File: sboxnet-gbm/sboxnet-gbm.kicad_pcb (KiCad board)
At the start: 2 copper layers, 102.4 x 85.1 mm, 47 parts, among them J1 Screw_Terminal_01x04, J2 Screw_Terminal_01x04, J3 Screw_Terminal_01x04, J4 sboxnet-stecker_02x17, J5 Screw_Terminal_01x04, U1 LTV-844, U2 LTV-844, U3 LTV-844, U4 SN65HVD230

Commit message: gbm
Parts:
- removed REF** (x4): MountingHole_2.2mm_M2, sboxnet:MountingHole_2.2mm_M2
- removed RN2: R_Network05, Resistor_THT:R_Array_SIP6
- removed TH0: Thermistor_PTC, Resistor_SMD:R_1206_3216Metric
- added J6: Conn_02x08_Top_Bottom, Connector_PinSocket_2.54mm:PinSocket_2x08_P2.54mm_Vertical, F.Cu at (136.9, 124.8)
- added JP1: SolderJumper_3_Open, Jumper:SolderJumper-3_P1.3mm_Open_RoundedPad1.0x1.5mm, F.Cu at (232.8, 67.2)
- added JP2: SolderJumper_3_Open, Jumper:SolderJumper-3_P1.3mm_Open_RoundedPad1.0x1.5mm, F.Cu at (183.1, 62.5)
- added JP3: SolderJumper_3_Open, Jumper:SolderJumper-3_P1.3mm_Open_RoundedPad1.0x1.5mm, F.Cu at (183.1, 66.3)
- added TH10: Thermistor_PTC, Resistor_SMD:R_1206_3216Metric, F.Cu at (263.6, 41.8)
- added TP10: TestPoint, Connector_PinHeader_2.54mm:PinHeader_1x01_P2.54mm_Vertical, F.Cu at (250.2, 59.1)
- added TP2: TestPoint, Connector_PinHeader_2.54mm:PinHeader_1x01_P2.54mm_Vertical, F.Cu at (263.1, 49.1)
- added TP3: TestPoint, Connector_PinHeader_2.54mm:PinHeader_1x01_P2.54mm_Vertical, F.Cu at (256.5, 55.8)
- added TP4: TestPoint, Connector_PinHeader_2.54mm:PinHeader_1x01_P2.54mm_Vertical, F.Cu at (250.2, 63.7)
- added TP5: TestPoint, Connector_PinHeader_2.54mm:PinHeader_1x01_P2.54mm_Vertical, F.Cu at (274.7, 35.9)
- added TP6: TestPoint, Connector_PinHeader_2.54mm:PinHeader_1x01_P2.54mm_Vertical, F.Cu at (268.8, 42.5)
- added TP7: TestPoint, Connector_PinHeader_2.54mm:PinHeader_1x01_P2.54mm_Vertical, F.Cu at (238.1, 71.0)
- added TP8: TestPoint, Connector_PinHeader_2.54mm:PinHeader_1x01_P2.54mm_Vertical, F.Cu at (226.7, 81.7)
- added TP9: TestPoint, Connector_PinHeader_2.54mm:PinHeader_1x01_P2.54mm_Vertical, F.Cu at (215.4, 93.7)
- BAR1: footprint Display:HDSP-4830 -> Package_DIP:DIP-20_W7.62mm_Socket
- D1, D10, D2, D3, D4, D5, D6, D7, D8, D9, TH1, TH2, TH3, TH4, TH5, TH6, TH7, TH8, TH9, U4: moved to F.Cu
- R1, R10, R2, R3, R4, R5, R6, R7, R8, R9: footprint Resistor_SMD:R_1206_3216Metric_Pad1.42x1.75mm_HandSolder -> Resistor_SMD:R_1206_3216Metric_Pad1.30x1.75mm_HandSolder; moved to F.Cu
- RN1: value R_Network05 -> R_Network15; footprint Resistor_THT:R_Array_SIP6 -> Package_SO:SOIC-16W_5.3x10.2mm_P1.27mm; moved to B.Cu
- moved TH7 217.8 mm to (269.6, 35.2), turned to 0 degrees
- moved D6 199.1 mm to (254.7, 48.5)
- moved TH6 199.0 mm to (263.6, 38.5), turned to 0 degrees
- moved TP1 182.9 mm to (244.6, 64.4)
- moved R6 175.8 mm to (233.0, 49.2), turned to 0 degrees
- moved TH3 160.8 mm to (263.6, 45.1), turned to 0 degrees
- moved U1 159.6 mm to (220.8, 49.6), turned to 0 degrees
- moved D3 153.4 mm to (236.2, 60.5)
- moved TH1 152.6 mm to (269.2, 38.5), turned to 0 degrees
- moved TH4 143.3 mm to (238.5, 67.1), turned to 0 degrees
- moved D5 134.1 mm to (205.1, 74.9)
- moved R7 130.4 mm to (263.8, 35.2)
- moved J3 128.3 mm to (218.8, 40.6)
- moved TH2 127.4 mm to (245.1, 60.4), turned to 0 degrees
- moved TH5 126.4 mm to (210.2, 91.5), turned to 0 degrees
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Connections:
- BAR1 pad 1: PD0 -> PC7
- BAR1 pad 10: PC7 -> PD0
- BAR1 pad 11: Net-(BAR1-Pad11) -> /L10
- BAR1 pad 12: Net-(BAR1-Pad12) -> /L9
- BAR1 pad 13: Net-(BAR1-Pad13) -> /L8
- BAR1 pad 14: Net-(BAR1-Pad14) -> /L7
- BAR1 pad 15: Net-(BAR1-Pad15) -> /L6
- BAR1 pad 16: Net-(BAR1-Pad16) -> /L5
- BAR1 pad 17: Net-(BAR1-Pad17) -> /L4
- BAR1 pad 18: Net-(BAR1-Pad18) -> /L3
- BAR1 pad 19: Net-(BAR1-Pad19) -> /L2
- BAR1 pad 2: PD1 -> PC6
- BAR1 pad 20: Net-(BAR1-Pad20) -> /L1
- BAR1 pad 3: PD2 -> PD7
- BAR1 pad 4: PD3 -> PD6
- BAR1 pad 5: PD4 -> PD5
- BAR1 pad 6: PD5 -> PD4
- BAR1 pad 7: PD6 -> PD3
- BAR1 pad 8: PD7 -> PD2
- BAR1 pad 9: PC6 -> PD1
- J4 pad 1: Net-(J4-Pad1) -> unconnected-(J4-Pad1)
- J4 pad 13: DCC_SENS -> PB0
- J4 pad 14: +3V3 -> PB1
- J4 pad 15: GNDPWR -> PB2
- J4 pad 16: +3V3 -> unconnected-(J4-Pad16)
- J4 pad 19: Net-(J4-Pad19) -> unconnected-(J4-Pad19)
- J4 pad 20: Net-(J4-Pad20) -> unconnected-(J4-Pad20)
- J4 pad 21: Net-(J4-Pad21) -> DCC_SENS
- J4 pad 22: Net-(J4-Pad22) -> unconnected-(J4-Pad22)
- J4 pad 4: Net-(J4-Pad4) -> unconnected-(J4-Pad4)
- J5 pad 3: Net-(J5-Pad3) -> unconnected-(J5-Pad3)
- J5 pad 4: Net-(J5-Pad4) -> unconnected-(J5-Pad4)
- R3 pad 2: Net-(D4-Pad3) -> Net-(D3-Pad3)
- R4 pad 2: Net-(D5-Pad3) -> Net-(D4-Pad3)
- R5 pad 2: Net-(D3-Pad3) -> Net-(D5-Pad3)
- RN1 pad 1: GNDPWR -> /L1
- RN1 pad 2: Net-(BAR1-Pad20) -> /L2
- RN1 pad 3: Net-(BAR1-Pad19) -> /L3
- RN1 pad 4: Net-(BAR1-Pad18) -> /L4
- RN1 pad 5: Net-(BAR1-Pad17) -> /L5
- RN1 pad 6: Net-(BAR1-Pad16) -> /L6
- TH1 pad 1: Net-(D8-Pad3) -> Net-(D1-Pad3)
- TH1 pad 2: S6 -> S0
- TH2 pad 2: S5 -> S1
- TH3 pad 1: Net-(D1-Pad3) -> Net-(D3-Pad3)
- TH3 pad 2: S4 -> S2
- TH5 pad 1: Net-(D3-Pad3) -> Net-(D5-Pad3)
- TH5 pad 2: S2 -> S4
- TH6 pad 1: Net-(D5-Pad3) -> Net-(D6-Pad3)
- TH6 pad 2: S1 -> S5
- TH7 pad 1: Net-(D6-Pad3) -> Net-(D7-Pad3)
- TH7 pad 2: S0 -> S6
- TH8 pad 1: Net-(D9-Pad3) -> Net-(D8-Pad3)
- TH8 pad 2: S9 -> S7
- TH9 pad 1: Net-(D10-Pad3) -> Net-(D9-Pad3)
- U1 pad 1: Net-(R6-Pad1) -> Net-(R1-Pad1)
- U1 pad 3: Net-(R4-Pad1) -> Net-(R2-Pad1)
- U1 pad 5: Net-(R5-Pad1) -> Net-(R3-Pad1)
- U1 pad 7: Net-(R3-Pad1) -> Net-(R4-Pad1)
- U2 pad 1: Net-(R1-Pad1) -> Net-(R5-Pad1)
- U2 pad 3: Net-(R2-Pad1) -> Net-(R6-Pad1)
- U2 pad 5: Net-(R8-Pad1) -> Net-(R7-Pad1)
- U2 pad 7: Net-(R7-Pad1) -> Net-(R8-Pad1)
- U3 pad 1: Net-(R10-Pad1) -> Net-(R9-Pad1)
- U3 pad 10: (no net) -> unconnected-(U3-Pad10)
- U3 pad 11: (no net) -> unconnected-(U3-Pad11)
- U3 pad 12: (no net) -> unconnected-(U3-Pad12)
- U3 pad 3: Net-(R9-Pad1) -> Net-(R10-Pad1)
- U3 pad 5: (no net) -> unconnected-(U3-Pad5)
- U3 pad 6: (no net) -> unconnected-(U3-Pad6)
- U3 pad 7: (no net) -> unconnected-(U3-Pad7)
- U3 pad 8: (no net) -> unconnected-(U3-Pad8)
- U3 pad 9: (no net) -> unconnected-(U3-Pad9)
- U4 pad 1: Net-(U4-Pad1) -> unconnected-(U4-Pad1)
- U4 pad 5: Net-(U4-Pad5) -> unconnected-(U4-Pad5)
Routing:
- net SGND1: track 430.8 -> 0.00 mm
- net GNDPWR: track 275.2 -> 78.1 mm
- net PD5: track 45.6 -> 121.3 mm
- net PD4: track 41.7 -> 114.8 mm
- net PD3: track 43.4 -> 110.0 mm, vias 0 -> 1
- net PD2: track 39.3 -> 105.3 mm
- net +3V3: track 56.7 -> 0.00 mm
- net PC1: track 55.0 -> 0.00 mm
- net PC0: track 48.1 -> 0.00 mm
- net DCC_SENS: track 42.5 -> 0.00 mm
- net Net-(R10-Pad1): track 40.2 -> 0.00 mm
- net S0: track 38.3 -> 0.00 mm
- net Net-(D8-Pad3): track 37.9 -> 0.00 mm
- net PA7: track 37.5 -> 0.00 mm
- net Net-(D7-Pad3): track 34.5 -> 0.00 mm
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- removed copper zone on B.Cu, net GNDPWR
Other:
- board outline removed
- net class Default removed
- rule pad_to_mask_clearance: 0.051 -> 0
- board text removed: "(c) 09.07.2020 Thomas Maier"
- board text removed: "0"
- board text removed: "1"
- board text removed: "2"
- board text removed: "3"
- board text removed: "4"
- board text removed: "5"
- board text removed: "6"
- board text removed: "7"
- board text removed: "8"
- board text removed: "9"
- board text removed: "SGND"
- board text removed: "Sboxnet GBM 2"
- board text removed: "tom@tom.ist-im-web.de"

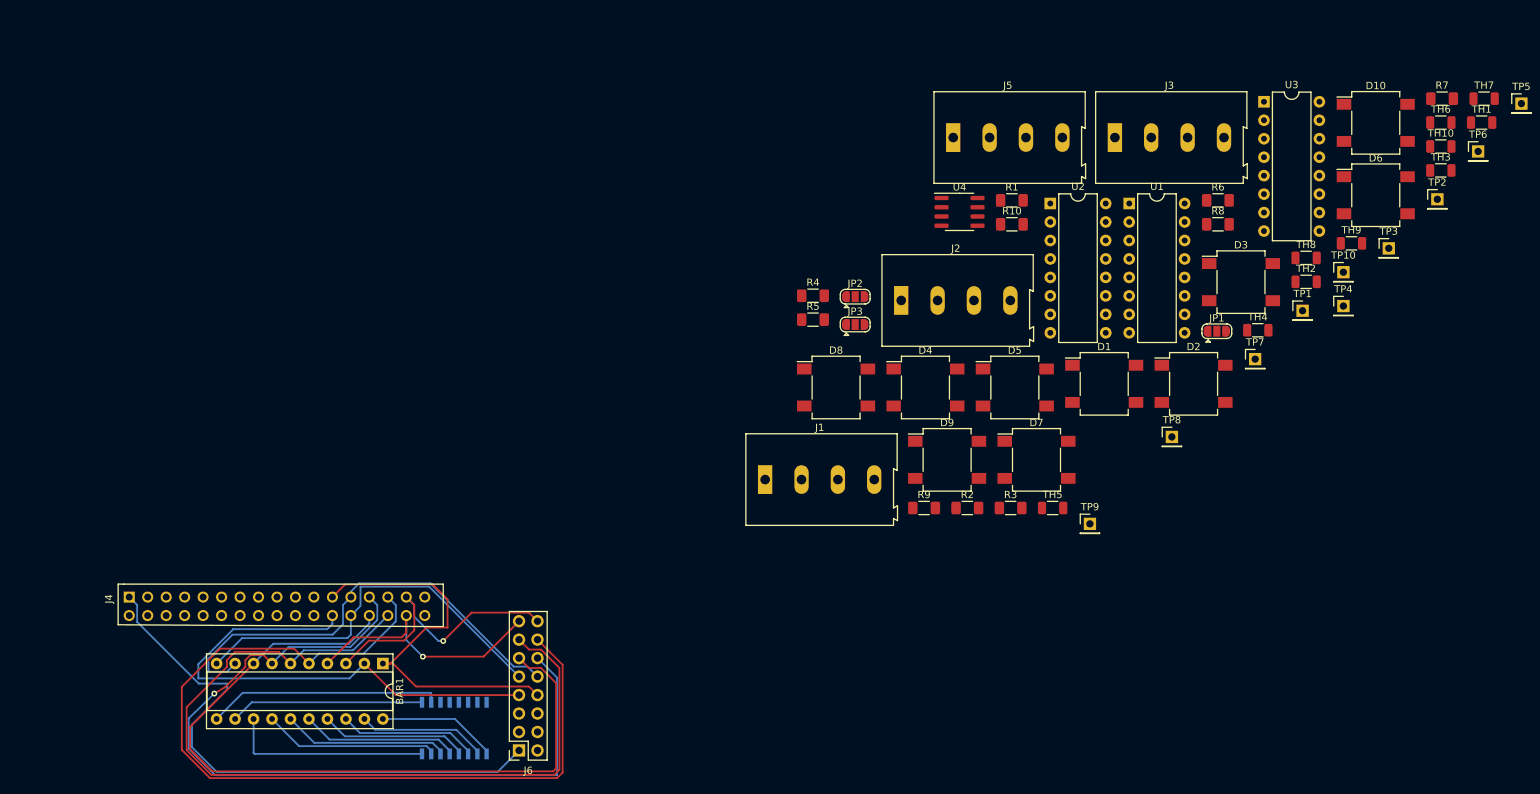
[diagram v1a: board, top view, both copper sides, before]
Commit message: kicad 5 -> 6
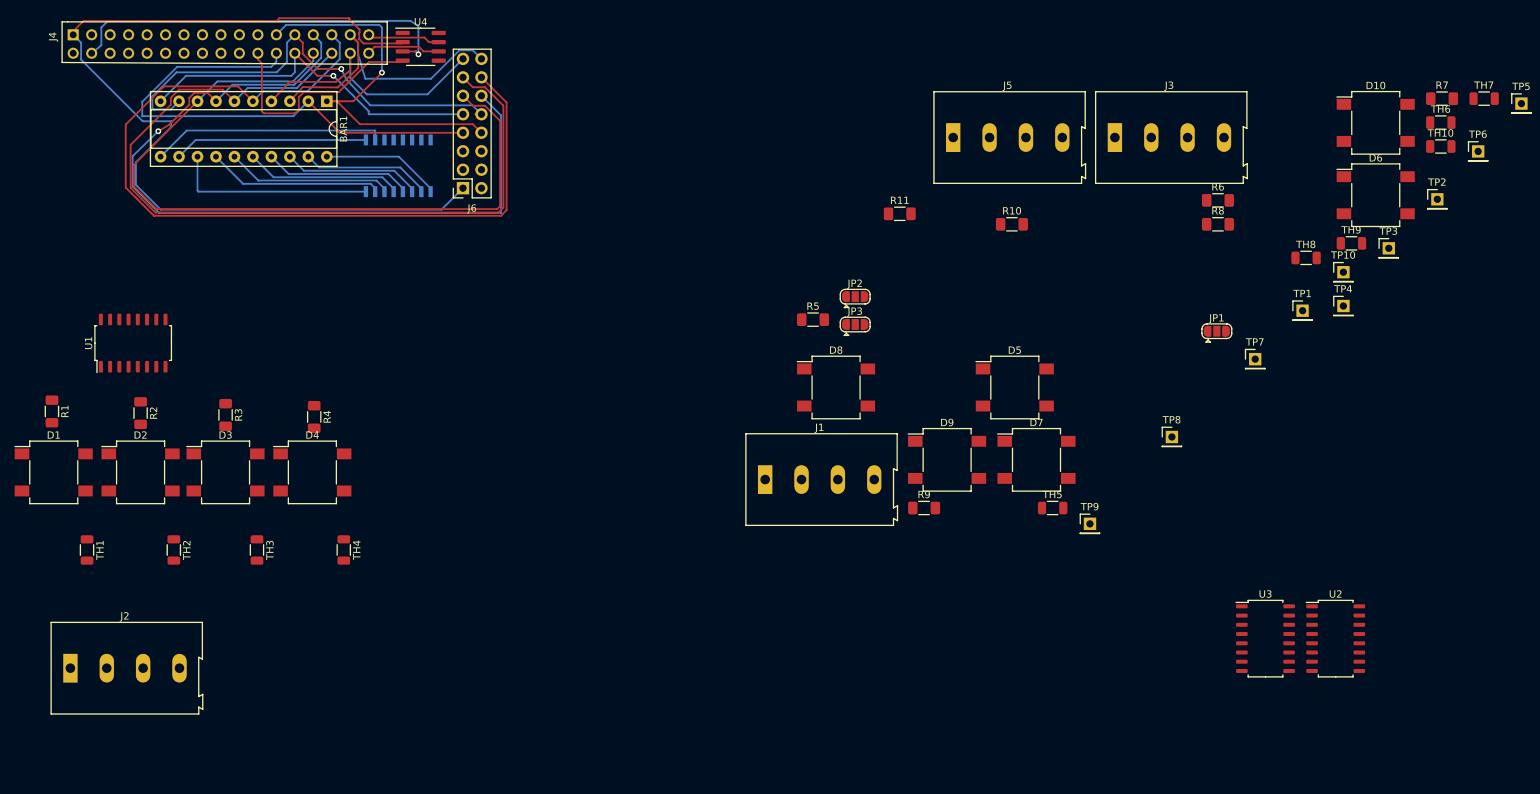
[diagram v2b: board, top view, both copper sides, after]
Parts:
- added R11: 0, Resistor_SMD:R_1206_3216Metric_Pad1.30x1.75mm_HandSolder, F.Cu at (189.2, 51.1)
- U1, U2, U3: footprint Package_DIP:DIP-16_W7.62mm -> Package_SO:SOIC-16_4.55x10.3mm_P1.27mm
- moved TH1 200.6 mm to (77.5, 97.3), turned to -90 degrees
- moved TH3 171.0 mm to (100.8, 97.3), turned to -90 degrees
- moved TH2 160.0 mm to (89.4, 97.3), turned to -90 degrees
- moved D2 145.3 mm to (84.8, 86.6)
- moved D1 145.0 mm to (72.9, 86.6)
- moved D3 142.1 mm to (96.5, 86.6)
- moved U1 138.3 mm to (83.8, 68.8), turned to 90 degrees
- moved R1 135.2 mm to (72.6, 78.2), turned to -90 degrees
- moved TH4 129.3 mm to (112.8, 97.3), turned to -90 degrees
- moved J2 124.9 mm to (75.2, 113.5)
- moved R2 114.4 mm to (84.8, 78.5), turned to -90 degrees
- moved R3 108.7 mm to (96.5, 78.7), turned to -90 degrees
- moved D4 85.1 mm to (108.5, 86.6)
- moved BAR1 77.7 mm to (110.4, 35.6)
- moved RN1 77.7 mm to (120.3, 44.5)
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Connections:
- U4 pad 8: GNDPWR -> Net-(U4-Pad8)
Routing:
- net +3V3: track 0.00 -> 54.7 mm, vias 0 -> 1
- net GNDPWR: track 78.1 -> 127.1 mm
- net DCC_SENS: track 0.00 -> 31.7 mm
- net DCC_A: track 0.00 -> 10.3 mm
- net DCC_B: track 0.00 -> 10.0 mm
- net PD0: track 54.2 -> 49.6 mm, vias 0 -> 1
- net PC7: track 55.3 -> 53.7 mm, vias 0 -> 1
- net PD7: track 39.9 -> 41.1 mm, vias 1 -> 0
- net PD1: track 62.7 -> 62.8 mm, vias 0 -> 1
- net PD6: track 36.8 -> 36.7 mm, vias 1 -> 0

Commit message: cleanup
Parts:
- JP1, JP2, JP3: value SolderJumper_3_Open -> SolderJumper_2_Open; footprint Jumper:SolderJumper-3_P1.3mm_Open_RoundedPad1.0x1.5mm -> Jumper:SolderJumper-2_P1.3mm_Open_TrianglePad1.0x1.5mm
- RN1: moved to F.Cu
- moved TH7 225.6 mm to (67.2, 135.0), turned to -90 degrees
- moved TP2 223.4 mm to (43.8, 91.0)
- moved TH6 223.3 mm to (62.2, 135.0), turned to -90 degrees
- moved TP5 211.2 mm to (71.0, 91.5)
- moved TP1 211.1 mm to (35.2, 91.0)
- moved TP3 207.0 mm to (52.5, 91.2)
- moved TH10 202.4 mm to (84.2, 135.5), turned to -90 degrees
- moved R7 199.4 mm to (87.0, 127.5), turned to -90 degrees
- moved TP6 194.4 mm to (80.8, 92.0)
- moved J3 192.7 mm to (57.2, 145.5)
- moved TP4 190.0 mm to (62.2, 91.2)
- moved TH9 189.8 mm to (79.2, 135.3), turned to -90 degrees
- moved TH8 189.4 mm to (72.5, 135.0), turned to -90 degrees
- moved JP1 188.5 mm to (44.5, 74.0), turned to 180 degrees
- moved D6 186.9 mm to (80.2, 115.5), turned to -90 degrees
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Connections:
- JP1 pad 1: GNDPWR -> PB2
- JP1 pad 2: PB2 -> GNDPWR
- JP2 pad 1: GNDPWR -> PB1
- JP2 pad 2: PB1 -> GNDPWR
- JP3 pad 1: GNDPWR -> PB0
- JP3 pad 2: PB0 -> GNDPWR
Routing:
- net SGND1: track 0.00 -> 235.1 mm
- net PC1: track 0.00 -> 84.4 mm
- net PC0: track 0.00 -> 72.1 mm
- net PD5: track 121.3 -> 49.8 mm
- net PA7: track 0.00 -> 71.1 mm
- net PD4: track 114.8 -> 49.0 mm
- net PA6: track 0.00 -> 61.9 mm
- net PA5: track 0.00 -> 58.4 mm
- net PA3: track 0.00 -> 53.5 mm
- net PD2: track 105.3 -> 52.9 mm
- net PA4: track 0.00 -> 51.8 mm
- net PD3: track 110.0 -> 61.6 mm, vias 1 -> 0
- net PA0: track 0.00 -> 46.7 mm
- net GNDPWR: track 127.1 -> 173.6 mm
- net PA1: track 0.00 -> 43.3 mm
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- added copper zone on B.Cu, net GNDPWR
- added copper zone on F.Cu, net GNDPWR
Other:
- board outline added: 91.5 x 93.5 mm
